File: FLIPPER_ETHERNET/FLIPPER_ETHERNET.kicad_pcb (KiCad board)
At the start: 2 copper layers, 67 x 25 mm, 33 parts, among them J1 RJ45_Hanrun_HR911105A_Horizon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, J2 Conn_01x08_Socket, J3 Conn_01x10_Socket, SW1 SW_Push, U1 ENC28J60x-ML, Y1 25MHz

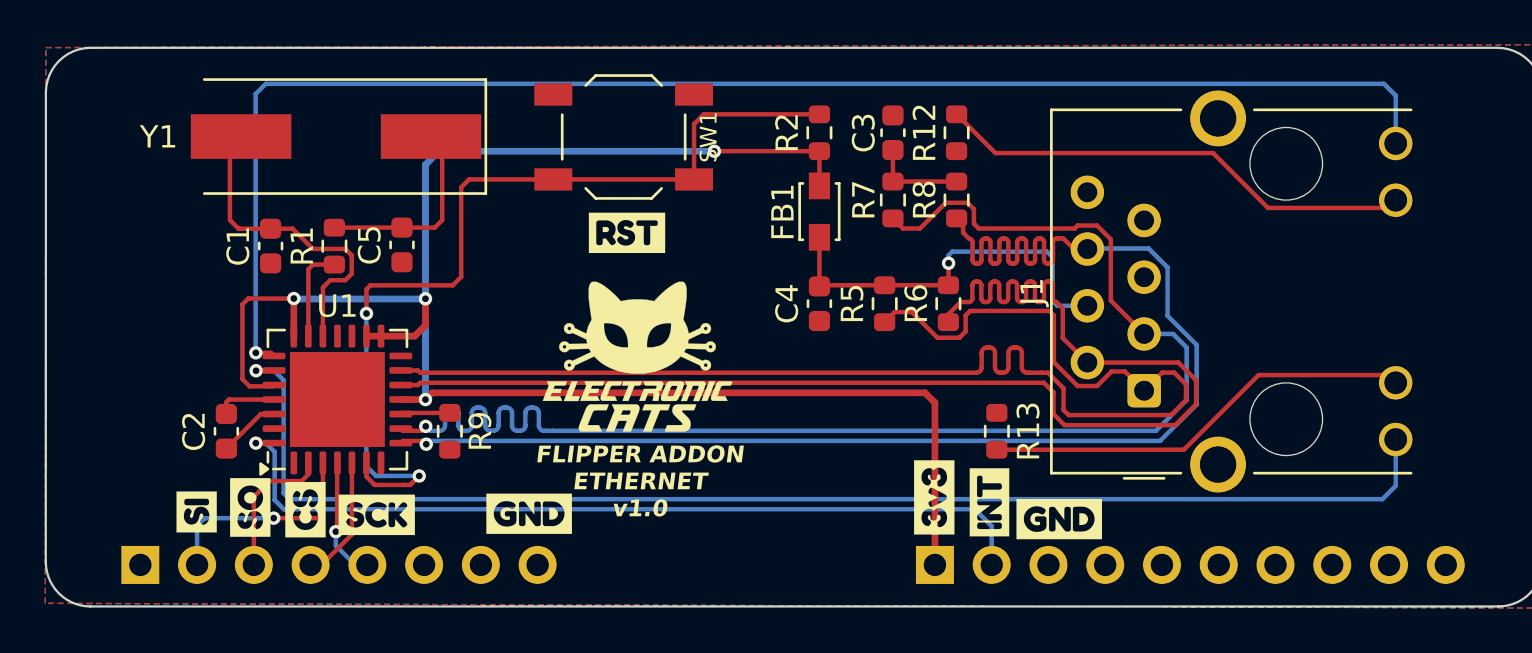
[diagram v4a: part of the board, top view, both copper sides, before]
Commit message: feat: decoupling capacitors moved, labels modified
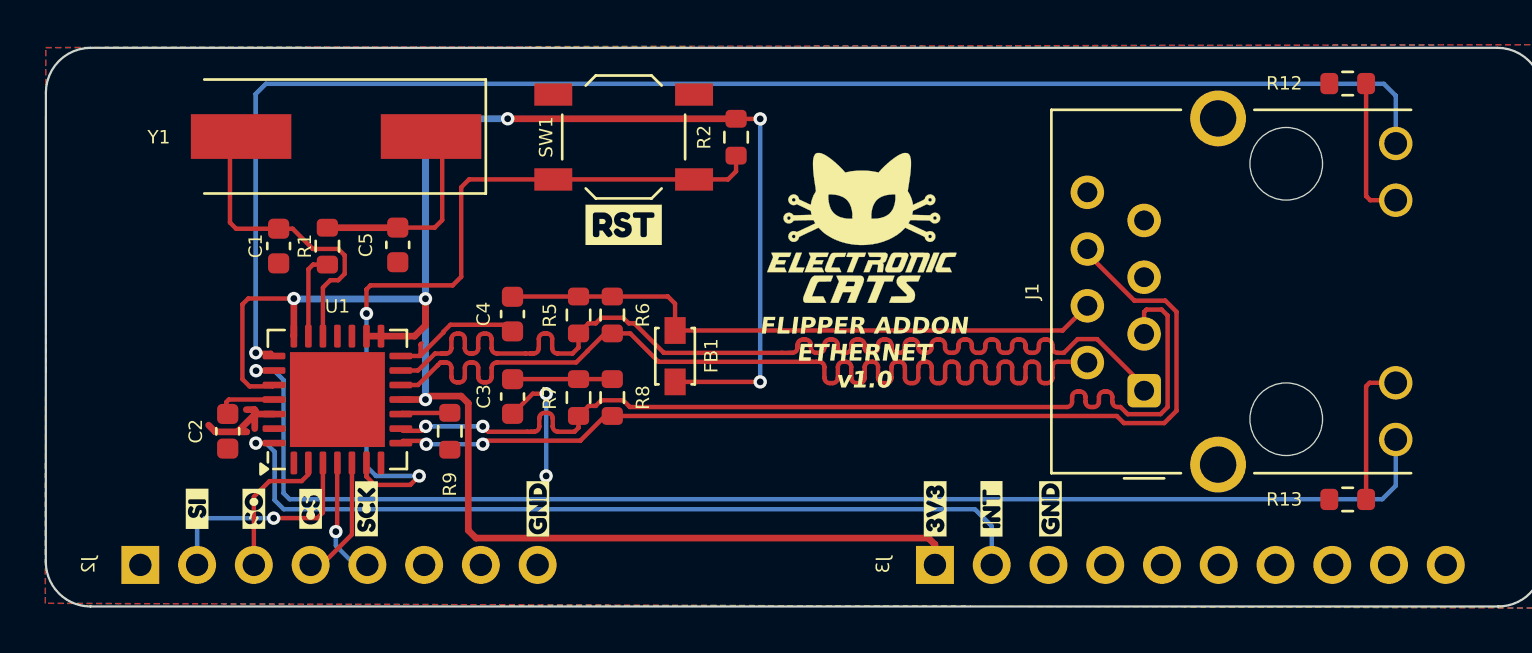
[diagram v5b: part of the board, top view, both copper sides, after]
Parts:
- removed kibuzzard-670697AB: G***, kibuzzard-670697AB
- removed kibuzzard-670697C4: G***, kibuzzard-670697C4
- removed kibuzzard-670697CE: G***, kibuzzard-670697CE
- removed kibuzzard-670697DC: G***, kibuzzard-670697DC
- removed kibuzzard-6706980D: G***, kibuzzard-6706980D
- removed kibuzzard-6706982B: G***, kibuzzard-6706982B
- removed kibuzzard-67069833: G***, kibuzzard-67069833
- removed kibuzzard-67069840: G***, kibuzzard-67069840
- added kibuzzard-6706FBB6: G***, kibuzzard-6706FBB6, F.Cu at (161.0, 65.8)
- added kibuzzard-6706FBB6: G***, kibuzzard-6706FBB6, F.Cu at (138.1, 65.8)
- added kibuzzard-6706FC38: G***, kibuzzard-6706FC38, F.Cu at (158.3, 65.8)
- added kibuzzard-6706FD0C: G***, kibuzzard-6706FD0C, F.Cu at (130.4, 65.8)
- added kibuzzard-6706FE25: G***, kibuzzard-6706FE25, F.Cu at (155.8, 65.8)
- added kibuzzard-6706FEBD: G***, kibuzzard-6706FEBD, F.Cu at (122.8, 65.8)
- added kibuzzard-6706FECB: G***, kibuzzard-6706FECB, F.Cu at (125.3, 65.8)
- added kibuzzard-6706FEE4: G***, kibuzzard-6706FEE4, F.Cu at (127.9, 65.8)
- moved C3 20.7 mm to (136.9, 60.7), turned to -90 degrees
- moved R8 17.8 mm to (141.4, 60.8)
- moved R12 17.6 mm to (174.3, 46.7), turned to 180 degrees
- moved R7 16.6 mm to (139.9, 60.8)
- moved R13 16.0 mm to (174.3, 65.3), turned to 180 degrees
- moved R6 15.0 mm to (141.4, 57.1)
- moved C4 13.7 mm to (136.9, 57.0)
- moved R5 13.7 mm to (139.9, 57.1)
- moved G*** 11.6 mm to (152.6, 53.2)
- moved FB1 9.14 mm to (144.2, 58.9), turned to 90 degrees
- moved R2 3.74 mm to (146.9, 49.1), turned to -90 degrees
- moved kibuzzard-6706978D 0.39 mm to (141.9, 53.0)
- moved C1 0.36 mm to (126.5, 54.0)
- moved R1 0.31 mm to (128.6, 54.0)
- moved C5 0.19 mm to (131.8, 54.0)
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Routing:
- net /RD+: track 63.4 -> 45.2 mm, vias 1 -> 2
- net /RD-: track 63.4 -> 46.1 mm, vias 1 -> 2
- net Net-(J1-Pad11): track 21.5 -> 6.92 mm
- net GND: track 2.77 -> 17.1 mm, vias 0 -> 2
- net Net-(J1-Pad10): track 19.4 -> 6.94 mm
- net +3.3V: track 80.4 -> 92.7 mm, vias 4 -> 6
- net /TD+: track 60.0 -> 47.9 mm
- net /TD-: track 60.0 -> 48.0 mm
- net /TCT: track 17.8 -> 27.6 mm, vias 1 -> 0
- net /RESET: track 41.1 -> 35.5 mm
- net /OSC1: track 15.0 -> 14.5 mm

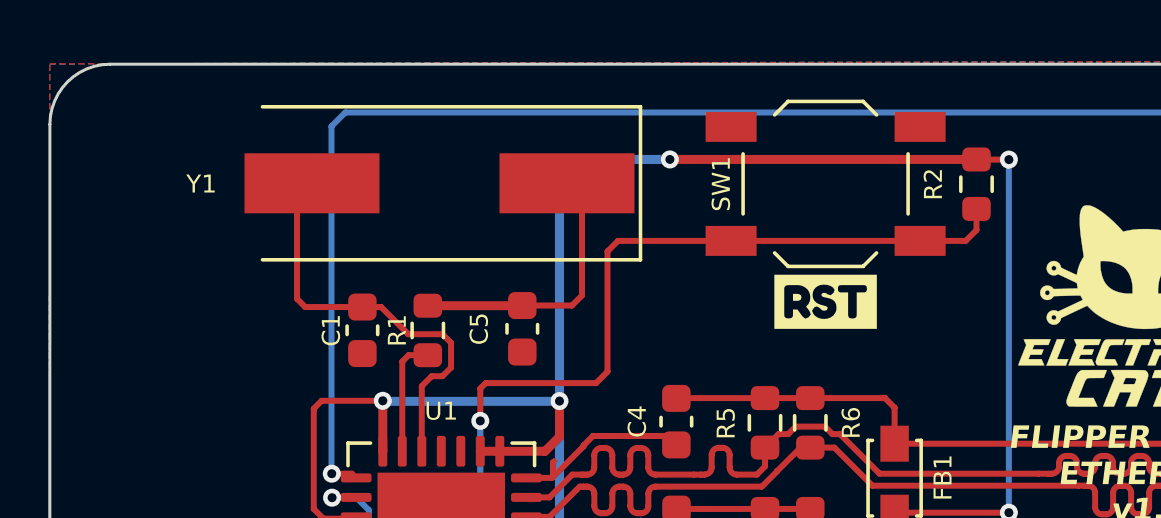
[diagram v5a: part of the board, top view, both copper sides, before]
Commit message: feat: bom added
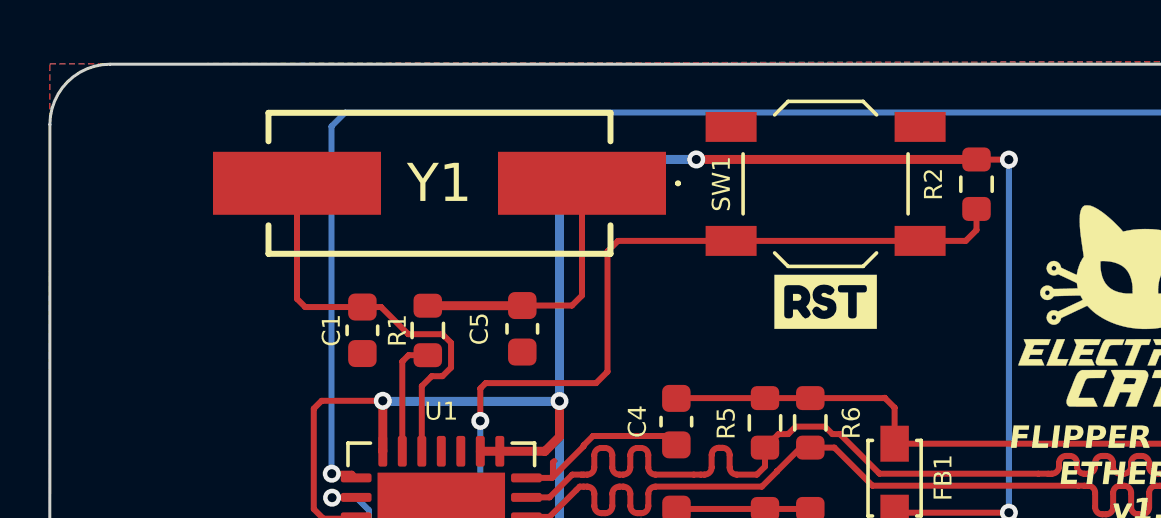
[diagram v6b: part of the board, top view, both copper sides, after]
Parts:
- Y1: footprint Crystal:Crystal_SMD_HC49-SD -> FLIPPER_ETHERNET:ABLS-25.000MHZ-20-F-T

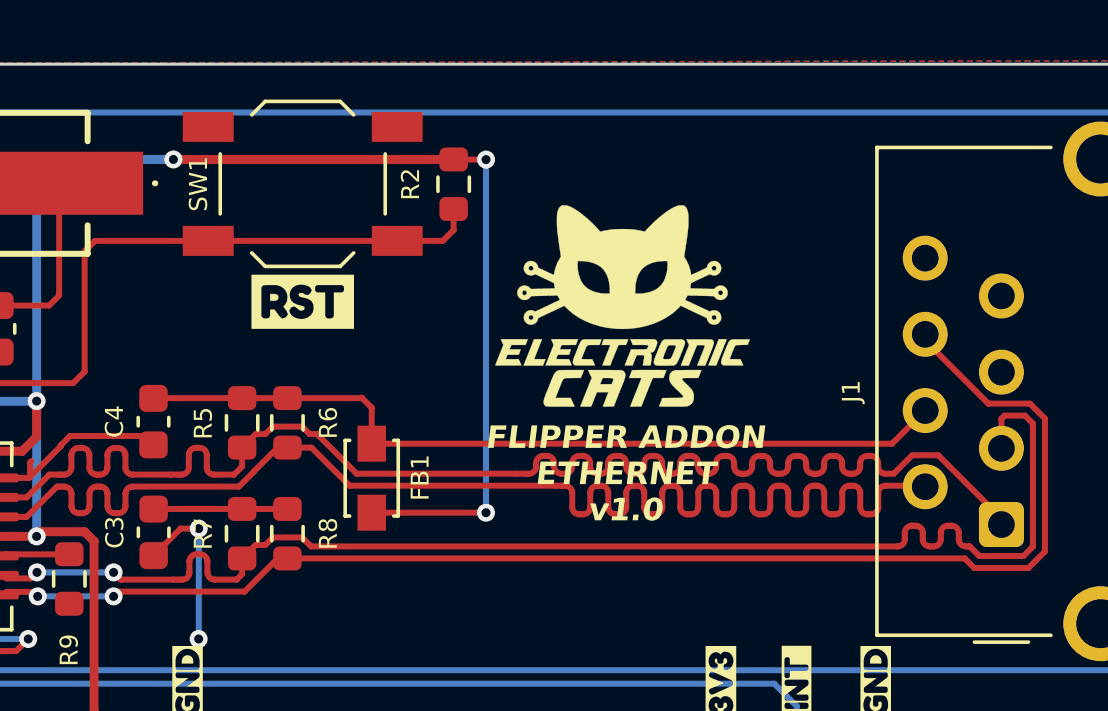
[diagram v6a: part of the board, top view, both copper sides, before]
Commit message: feat: bom corrected and change of model components components changed were SW1 and FB1
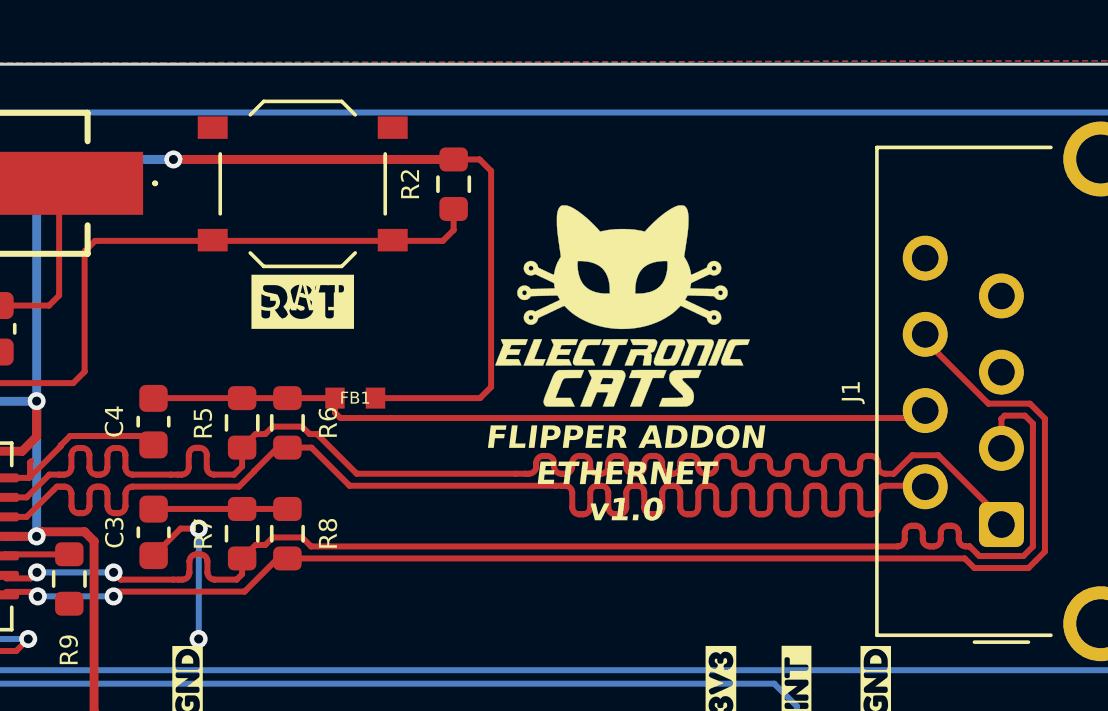
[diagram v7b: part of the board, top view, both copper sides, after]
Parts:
- FB1: value FerriteBead -> FerriteBead 80 mA; footprint Inductor_SMD:L_Walsin_WLFM201209x -> FLIPPER_ETHERNET:BLM18SP221SN1B
- SW1: footprint Button_Switch_SMD:SW_SPST_TL3342 -> Button_Switch_SMD:SW_Push_1P1T_XKB_TS-1187A
- moved FB1 2.73 mm to (143.6, 56.3), turned to 180 degrees
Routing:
- net +3.3V: track 92.7 -> 88.7 mm, vias 6 -> 4
- net /TCT: track 27.6 -> 26.5 mm

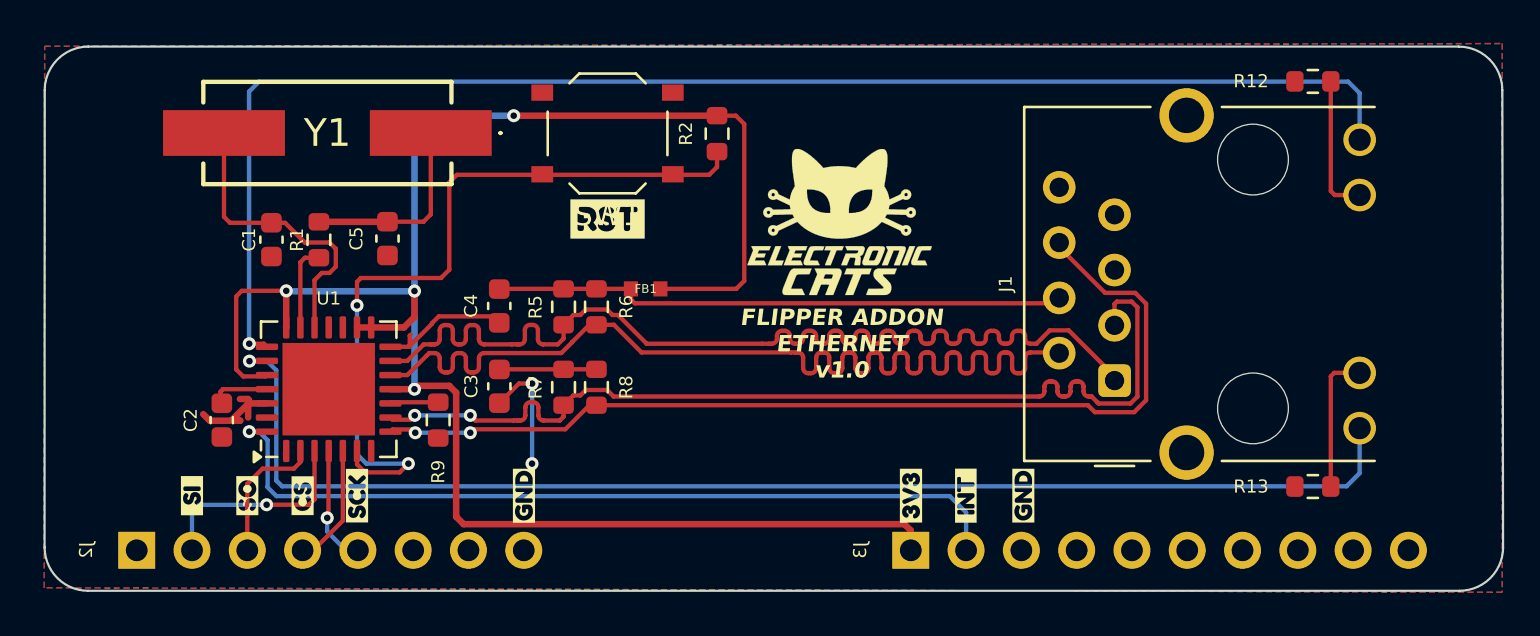
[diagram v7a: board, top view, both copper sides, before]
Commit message: feat: flipper ethernet pcb adapted in olimex pcb
All components passed behind the pcb except the
RJ45 and reset button

Decoupling capacitors of ENC28J60 added

Crystal changed for a smaller one
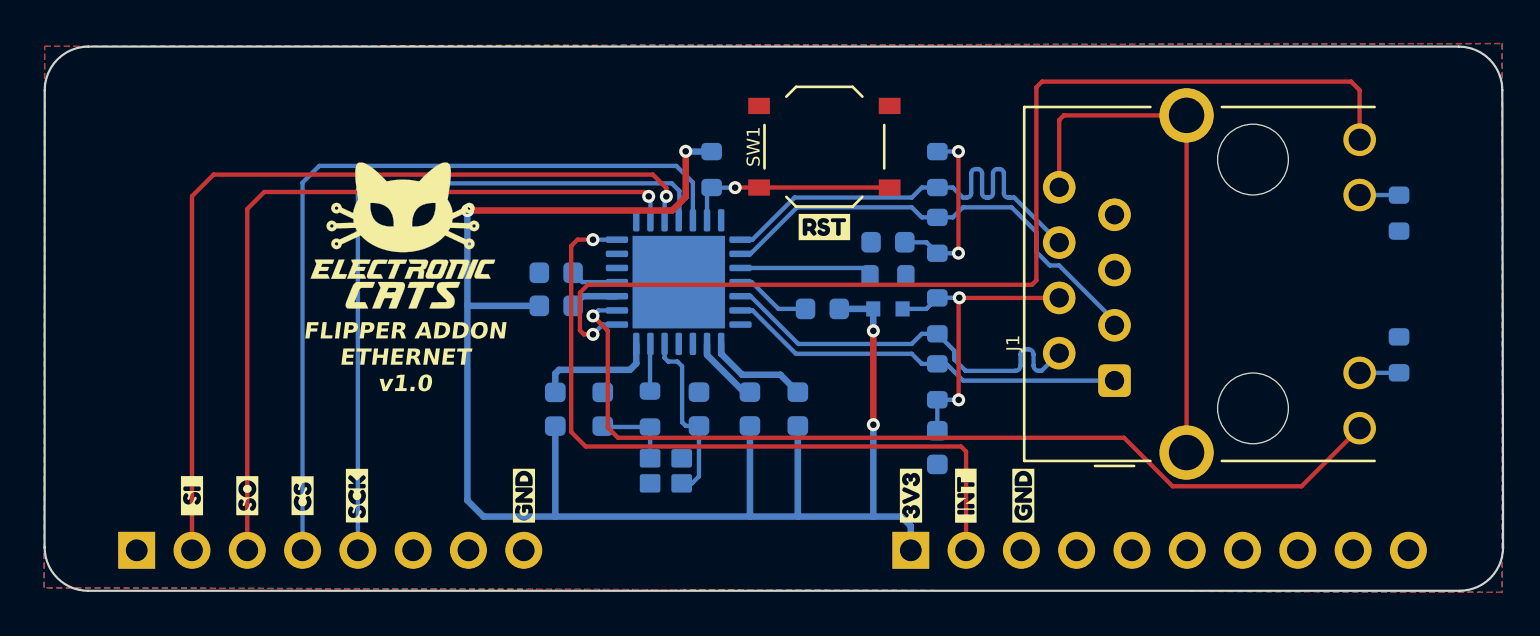
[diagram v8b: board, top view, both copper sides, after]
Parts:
- removed kibuzzard-6706978D: G***, kibuzzard-6706978D
- added C10: 0.1uF, Capacitor_SMD:C_0603_1608Metric, B.Cu at (139.5, 61.8)
- added C6: 0.1uF, Capacitor_SMD:C_0603_1608Metric, B.Cu at (151.8, 57.2)
- added C7: 0.1uF, Capacitor_SMD:C_0603_1608Metric, B.Cu at (150.6, 61.8)
- added C8: 0.1uF, Capacitor_SMD:C_0603_1608Metric, B.Cu at (139.5, 57.0)
- added C9: 0.1uF, Capacitor_SMD:C_0603_1608Metric, B.Cu at (148.4, 61.8)
- added kibuzzard-67102A6B: G***, kibuzzard-67102A6B, F.Cu at (151.8, 53.4)
- C1, C2, C3, C4, C5, FB1, R1, R12, R13, R2, R5, R6, R7, R8, R9, U1: moved to B.Cu
- Y1: footprint FLIPPER_ETHERNET:ABLS-25.000MHZ-20-F-T -> Crystal:Crystal_SMD_SeikoEpson_FA128-4Pin_2.0x1.6mm; moved to B.Cu
- moved REF** 31.1 mm to (121.7, 54.9)
- moved Y1 22.0 mm to (144.6, 64.6)
- moved R9 21.7 mm to (154.8, 55.6), turned to 0 degrees
- moved C4 21.2 mm to (157.0, 63.5)
- moved C1 21.1 mm to (146.1, 61.8), turned to 90 degrees
- moved G*** 20.1 mm to (132.5, 53.8)
- moved C3 19.0 mm to (154.8, 54.1), turned to 180 degrees
- moved R8 18.6 mm to (157.0, 50.8)
- moved R7 18.5 mm to (157.0, 53.8), turned to -90 degrees
- moved R5 17.5 mm to (157.0, 60.5), turned to -90 degrees
- moved R1 17.1 mm to (143.8, 61.8), turned to 90 degrees
- moved U1 16.8 mm to (145.2, 56.0), turned to -90 degrees
- moved C2 16.8 mm to (139.5, 55.5), turned to 180 degrees
- moved R6 15.7 mm to (157.0, 57.5)
- moved C5 12.6 mm to (141.7, 61.8), turned to 90 degrees
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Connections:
- J1 pad 8: GND -> Net-(J1-Pad8)
- J1 pad SH: GND -> Net-(J1-Pad8)
- U1 pad 11: +3.3V -> Net-(U1-VDDTX)
- U1 pad 15: +3.3V -> Net-(U1-VDDRX)
- U1 pad 16: +3.3V -> Net-(U1-VDDPLL)
- U1 pad 21: +3.3V -> Net-(U1-VDDOSC)
- U1 pad 24: +3.3V -> Net-(U1-VDD)
- Y1 pad 1: Net-(C5-Pad1) -> /OSC1
- Y1 pad 2: /OSC1 -> GND
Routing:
- net /CS: track 5.62 -> 37.2 mm
- net /SI: track 9.85 -> 40.2 mm
- net /TD-: track 48.0 -> 18.5 mm
- net /TD+: track 47.9 -> 18.5 mm
- net /SO: track 6.42 -> 35.7 mm, vias 0 -> 1
- net /SCK: track 5.50 -> 33.0 mm, vias 1 -> 0
- net /RESET: track 35.5 -> 9.78 mm, vias 2 -> 1
- net /RD-: track 46.1 -> 21.2 mm, vias 2 -> 0
- net Net-(J1-Pad8): track 0.00 -> 24.5 mm
- net /RD+: track 45.2 -> 21.4 mm, vias 2 -> 0
- net GND: track 17.1 -> 0.00 mm, vias 2 -> 0
- net /LEDA: track 59.5 -> 43.4 mm
- net /LEDB: track 66.0 -> 51.2 mm
- net +3.3V: track 88.7 -> 75.8 mm
- net /TCT: track 26.5 -> 14.5 mm, vias 0 -> 2
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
